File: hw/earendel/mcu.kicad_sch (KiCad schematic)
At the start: 1 part, among them U1 RP2040

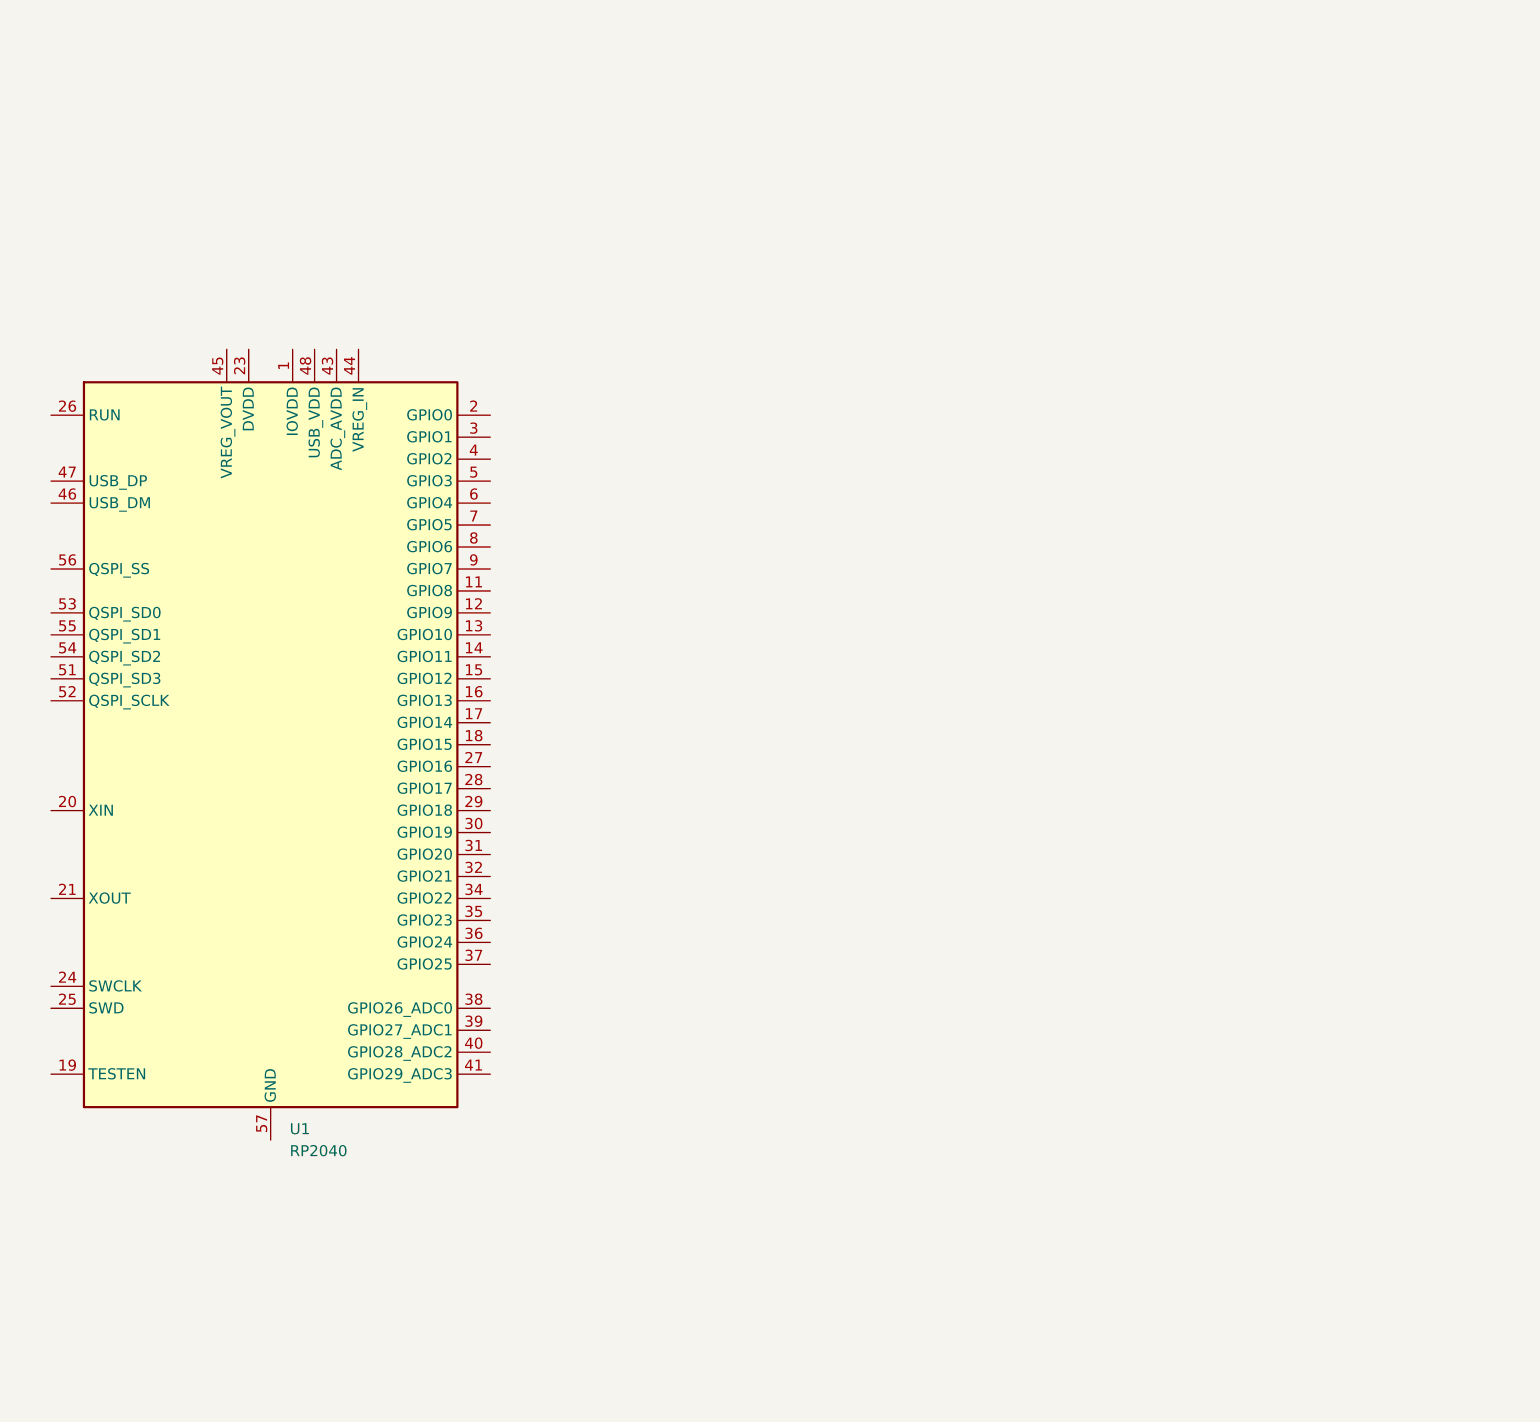
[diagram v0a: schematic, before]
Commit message: Added MCU decoupling caps, started power
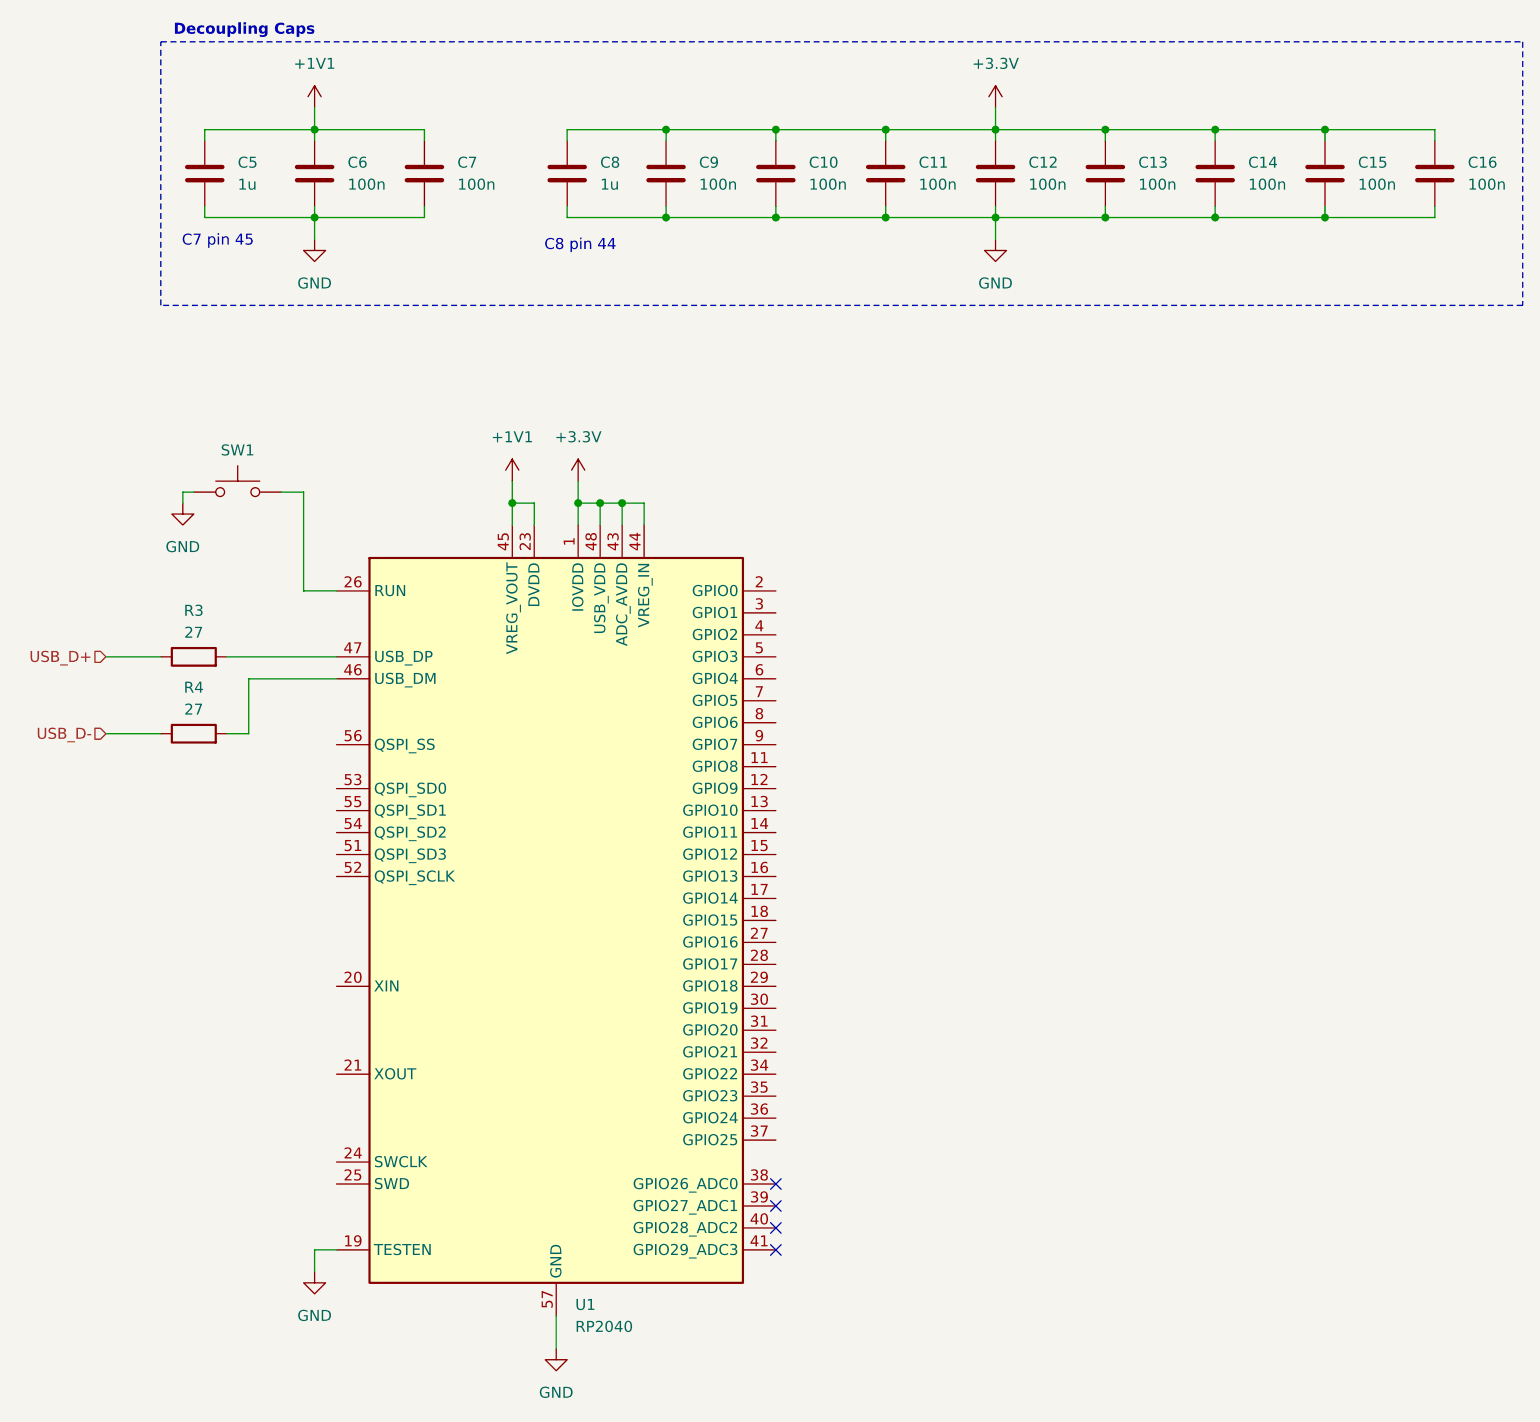
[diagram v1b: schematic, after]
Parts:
- added C10, C11, C12, C13, C14, C15, C16, C6, C7, C9: 100n, symbol Device:C
- added C5, C8: 1u, symbol Device:C
- added R3, R4: 27, symbol Device:R
- added SW1: SW_Push, symbol Switch:SW_Push
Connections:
- net +3.3V: now reaches U1.1 (IOVDD), U1.10 (IOVDD), U1.22 (IOVDD), U1.33 (IOVDD), U1.42 (IOVDD), U1.49 (IOVDD)
- net +3.3V: now also U1.43 (ADC_AVDD), U1.44 (VREG_IN), U1.48 (USB_VDD), C10.1, C11.1, C12.1, C13.1, C14.1, C15.1, C16.1, C8.1, C9.1
- net GND: now reaches U1.19 (TESTEN)
- net GND: now also U1.57 (GND), C10.2, C11.2, C12.2, C13.2, C14.2, C15.2, C16.2, C5.2, C6.2, C7.2, C8.2, C9.2, SW1.1
- net +1V1: now reaches U1.23 (DVDD), U1.50 (DVDD)
- net +1V1: now also U1.45 (VREG_VOUT), C5.1, C6.1, C7.1
- net at U1.26 (RUN): now also SW1.2
- net at U1.46 (USB_DM): now also R4.2
- net at U1.47 (USB_DP): now also R3.2
- new net USB_D+: R3.1
- new net USB_D-: R4.1
- no-connect marks 0 -> 4
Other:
- note added: "C7 pin 45"
- note added: "C8 pin 44"
- note added: "Decoupling Caps"
- moved on the sheet: U1
